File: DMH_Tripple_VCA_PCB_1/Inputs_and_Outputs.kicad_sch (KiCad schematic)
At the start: 0 parts

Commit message: Schematic in progress
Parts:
- added J1, J10, J2, J3, J4, J5, J6, J7, J8, J9: TS_Jack_6.35mm_Sw, SynthStuff:CUI_MJ-63052A, symbol SynthStuff:TS_Jack_6.35mm_Sw
- added J200: IDC_02x05, SynthStuff:IDC-Header_2x05_P2.54mm_Vertical_BackBone, symbol SynthStuff:BackBone_Connector_10Pin
- added J50, J60, J70: Conn_01x06, Connector_PinSocket_2.54mm:PinSocket_1x06_P2.54mm_Vertical, symbol Connector_Generic:Conn_01x06
- added R53, R54, R55: 20k, Resistor_THT:R_Axial_DIN0207_L6.3mm_D2.5mm_P7.62mm_Horizontal, symbol Device:R_US
- added RV4, RV5, RV6: 100k, SynthStuff:Potentiometer_Alpha_RD901F-40-00D_Single_Vertical, symbol Device:R_Potentiometer_US
- added SW1, SW2, SW3: SW_SPDT_321, symbol Switch:SW_SPDT_321
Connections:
- new net: J200.7 (Pin_7), J9.TN
- new net: J2.TN, J200.2 (Pin_2)
- new net: J1.TN, J200.1 (Pin_1)
- new net: J200.10 (Pin_10), J6.TN
- new net: J200.3 (Pin_3), J3.TN
- new net: J200.4 (Pin_4), J4.TN
- new net: J200.5 (Pin_5), J5.TN
- new net: J10.TN, J200.6 (Pin_6)
- new net: J200.8 (Pin_8), J8.TN
- new net: J200.9 (Pin_9), J7.TN
- new net: R54.1, RV5.1
- new net: R53.1, RV4.1
- new net: R55.1, RV6.1
- new net +12V: J50.1 (Pin_1), J60.1 (Pin_1), J70.1 (Pin_1), R53.2, R54.2, R55.2
- new net CV A Jack: J3.T
- new net CV B Jack: J6.T
- new net CV C Jack: J9.T
- new net GND: J1.S, J10.S, J2.S, J3.S, J4.S, J5.S, J50.5 (Pin_5), J50.6 (Pin_6), J6.S, J60.5 (Pin_5), J60.6 (Pin_6), J7.S, J70.5 (Pin_5), J70.6 (Pin_6), J8.S, J9.S, RV4.3, RV5.3, RV6.3
- new net Input A Jack: J1.T
- new net Input B Jack: J4.T
- new net Input C Jack: J7.T
- new net Mix Out Jack: J10.T
- new net Mute A Switch: J50.2 (Pin_2), SW1.3 (A)
- new net Mute B Switch: J60.2 (Pin_2), SW2.3 (A)
- new net Mute C Switch: J70.2 (Pin_2), SW3.3 (A)
- new net Offset A Pot: J50.4 (Pin_4), RV4.2
- new net Offset B Pot: J60.4 (Pin_4), RV5.2
- new net Offset C Pot: J70.4 (Pin_4), RV6.2
- new net Output A Jack: J2.T, J50.3 (Pin_3), SW1.2 (B)
- new net Output B Jack: J5.T, J60.3 (Pin_3), SW2.2 (B)
- new net Output C Jack: J70.3 (Pin_3), J8.T, SW3.2 (B)
- no-connect marks 0 -> 3
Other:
- note added: "PCB 2"

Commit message: Finished Schematic
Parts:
- removed SW2, SW3: SW_SPDT_321, symbol Switch:SW_SPDT_321
- added D3, D4, D5: LED_BGKR, LED_THT:LED_D5.0mm-4_RGB, symbol Device:LED_BGKR
- added R56, R58, R60: 220R, Resistor_THT:R_Axial_DIN0207_L6.3mm_D2.5mm_P7.62mm_Horizontal, symbol Device:R_US
- added R57, R59, R61: 330R, Resistor_THT:R_Axial_DIN0207_L6.3mm_D2.5mm_P7.62mm_Horizontal, symbol Device:R_US
- added SW2, SW3: SW_DPDT, SynthStuff:PinHeader_2x03_P2.54mm_Vertical_142536, symbol SynthStuff:Switch_DPDT
- SW1: value SW_SPDT_321 -> SW_DPDT; footprint (none) -> SynthStuff:PinHeader_2x03_P2.54mm_Vertical_142536; symbol Switch:SW_SPDT_321 -> SynthStuff:Switch_DPDT
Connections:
- net +12V: now also SW1.5 (B), SW2.5 (B), SW3.5 (B)
- net GND: now also D3.3 (K), D4.3 (K), D5.3 (K)
- net Mute A Switch: now also SW1.1 (A); no longer SW1.3 (A)
- net Mute B Switch: now also SW2.1 (A)
- net Mute C Switch: now also SW3.1 (A)
- net Output B Jack: now also SW2.2 (B)
- net Output C Jack: now also SW3.2 (B)
- new net: D4.2 (GA), R58.1
- new net: D4.4 (RA), R59.1
- new net: R57.2, SW1.4 (A)
- new net: R56.2, SW1.6 (C)
- new net: R61.2, SW3.4 (A)
- new net: R60.2, SW3.6 (C)
- new net: D3.2 (GA), R56.1
- new net: R59.2, SW2.4 (A)
- new net: R58.2, SW2.6 (C)
- new net: D5.2 (GA), R60.1
- new net: D3.4 (RA), R57.1
- new net: D5.4 (RA), R61.1
- no-connect marks 3 -> 6
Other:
- moved on the sheet: R53, R54, R55, RV4, RV5, RV6

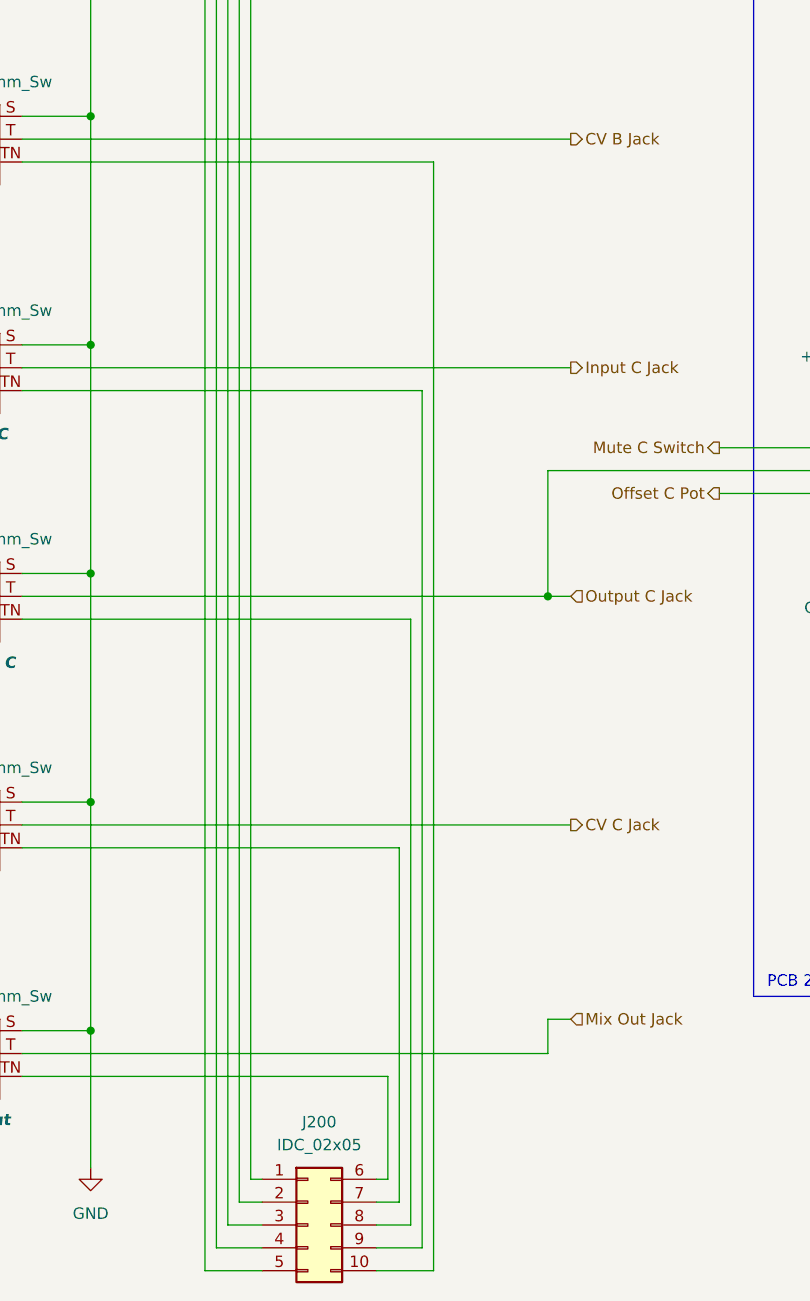
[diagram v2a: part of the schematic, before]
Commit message: PCB 1 component positioning ongoing
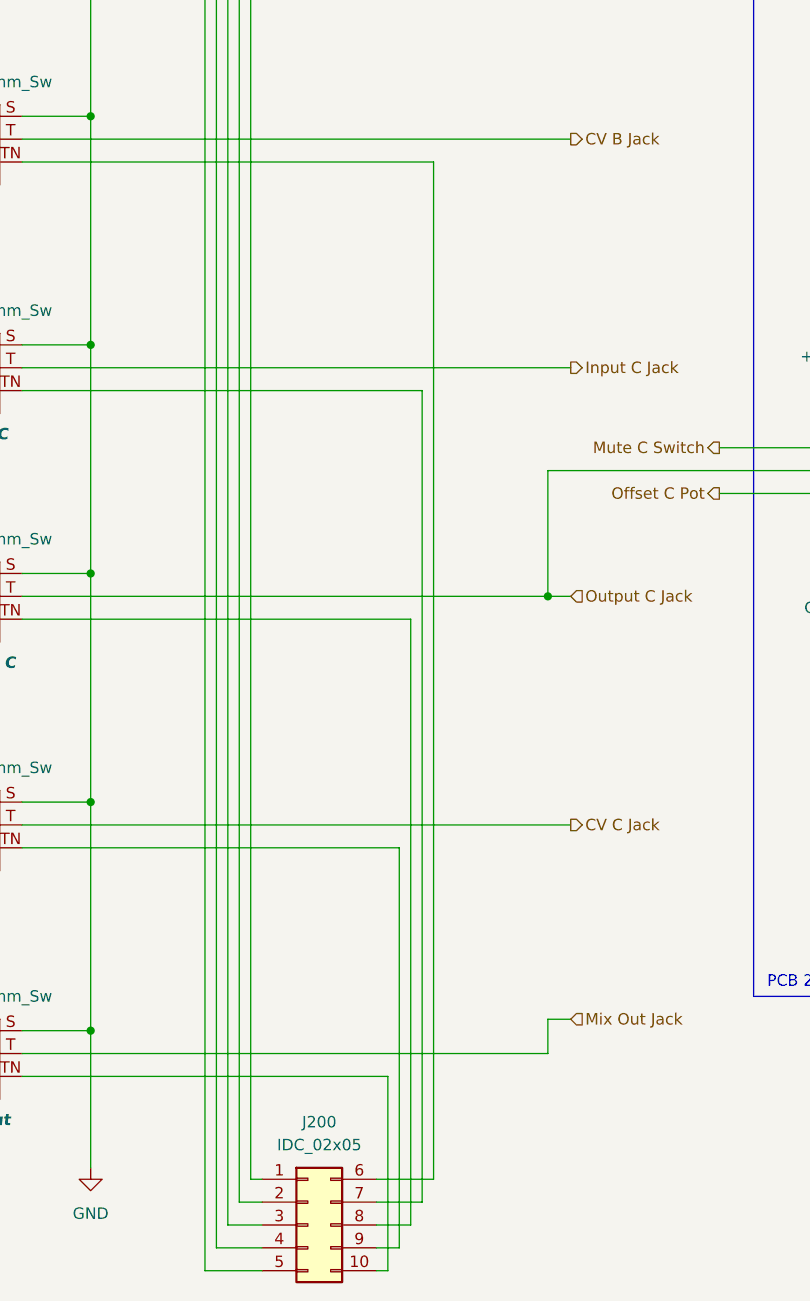
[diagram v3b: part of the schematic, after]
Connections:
- net at J9.TN: now also J200.9 (Pin_9); no longer J200.7 (Pin_7)
- net at J200.10 (Pin_10): now also J10.TN; no longer J6.TN
- net at J200.6 (Pin_6): now also J6.TN; no longer J10.TN
- net at J7.TN: now also J200.7 (Pin_7); no longer J200.9 (Pin_9)
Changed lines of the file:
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@@
+	(wire
+		(pts
+			(xy 69.85 270.51) (xy 74.93 270.51)
+		)
+		(stroke
+			(width 0)
+			(type default)
+		)
+	)
 	(wire
 		(pts
@@
 	(wire
 		(pts
+			(xy 69.85 267.97) (xy 76.2 267.97)
+		)
+		(stroke
+			(width 0)
+			(type default)
+		)
+	)
+	(wire
+		(pts
+			(xy 69.85 273.05) (xy 73.66 273.05)
+		)
+		(stroke
+			(width 0)
+			(type default)
+		)
+	)
+	(wire
+		(pts
 			(xy 176.53 146.05) (xy 179.07 146.05)
 		)
@@
 	(wire
 		(pts
-			(xy 72.39 270.51) (xy 72.39 231.14)
+			(xy 72.39 231.14) (xy 72.39 275.59)
 		)
 		(stroke
@@
 	(wire
 		(pts
-			(xy 69.85 278.13) (xy 76.2 278.13)
-		)
-		(stroke
-			(width 0)
-			(type default)
-		)
-	)
-	(wire
-		(pts
 			(xy 176.53 106.68) (xy 189.23 106.68)
 		)
@@
 	(wire
 		(pts
+			(xy 71.12 256.54) (xy 71.12 278.13)
+		)
+		(stroke
+			(width 0)
+			(type default)
+		)
+	)
+	(wire
+		(pts
 			(xy 52.07 104.14) (xy 30.48 104.14)
 		)
@@
 	(wire
 		(pts
-			(xy 71.12 256.54) (xy 71.12 267.97)
-		)
-		(stroke
-			(width 0)
-			(type default)
-		)
-	)
-	(wire
-		(pts
 			(xy 38.1 266.7) (xy 38.1 251.46)
 		)
@@
 	(wire
 		(pts
-			(xy 69.85 275.59) (xy 74.93 275.59)
-		)
-		(stroke
-			(width 0)
-			(type default)
-		)
-	)
-	(wire
-		(pts
 			(xy 158.75 195.58) (xy 158.75 209.55)
 		)
@@
 	(wire
 		(pts
+			(xy 72.39 275.59) (xy 69.85 275.59)
+		)
+		(stroke
+			(width 0)
+			(type default)
+		)
+	)
+	(wire
+		(pts
 			(xy 121.92 118.11) (xy 119.38 118.11)
 		)
@@
 	(wire
 		(pts
-			(xy 76.2 154.94) (xy 76.2 278.13)
+			(xy 76.2 154.94) (xy 76.2 267.97)
 		)
 		(stroke
@@
 	(wire
 		(pts
-			(xy 69.85 273.05) (xy 73.66 273.05)
-		)
-		(stroke
-			(width 0)
-			(type default)
-		)
-	)
-	(wire
-		(pts
 			(xy 146.05 67.31) (xy 146.05 72.39)
 		)
@@
 	(wire
 		(pts
-			(xy 74.93 180.34) (xy 74.93 275.59)
+			(xy 74.93 180.34) (xy 74.93 270.51)
 		)
 		(stroke
@@
 	(wire
 		(pts
-			(xy 69.85 267.97) (xy 71.12 267.97)
-		)
-		(stroke
-			(width 0)
-			(type default)
-		)
-	)
-	(wire
-		(pts
 			(xy 38.1 175.26) (xy 38.1 149.86)
 		)
@@
 	(wire
 		(pts
-			(xy 69.85 270.51) (xy 72.39 270.51)
-		)
-		(stroke
+			(xy 71.12 278.13) (xy 69.85 278.13)
+		)
+		(stroke

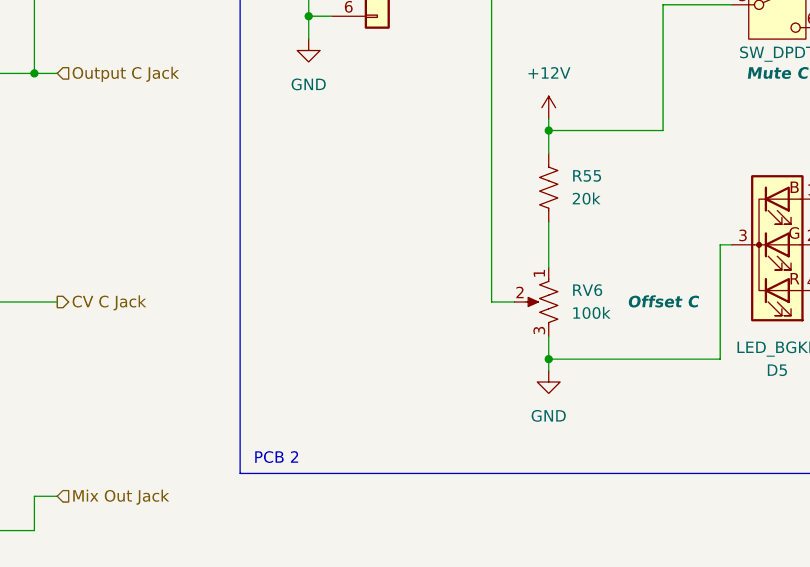
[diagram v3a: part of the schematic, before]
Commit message: PCB 1 component positioning in progress
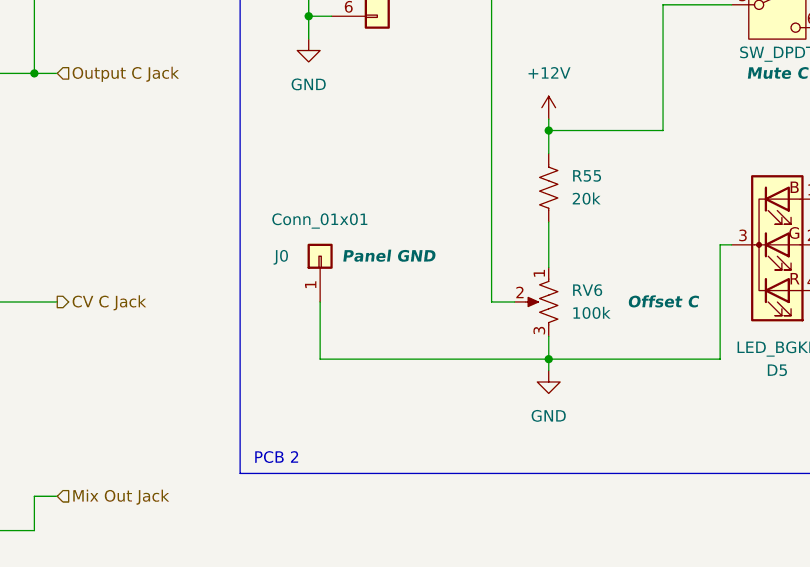
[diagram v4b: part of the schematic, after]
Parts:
- added J0: Conn_01x01, Connector_PinHeader_2.54mm:PinHeader_1x01_P2.54mm_Vertical, symbol Connector_Generic:Conn_01x01
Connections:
- net GND: now also J0.1 (Pin_1)
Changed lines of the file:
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@@
 	(wire
 		(pts
+			(xy 120.65 228.6) (xy 120.65 234.95)
+		)
+		(stroke
+			(width 0)
+			(type default)
+		)
+	)
+	(wire
+		(pts
 			(xy 121.92 194.31) (xy 119.38 194.31)
 		)
@@
 	(wire
 		(pts
+			(xy 120.65 234.95) (xy 146.05 234.95)
+		)
+		(stroke
+			(width 0)
+			(type default)
+		)
+	)
+	(wire
+		(pts
 			(xy 152.4 189.23) (xy 121.92 189.23)
 		)
@@
 					(unit 1)
 				)
+			)
+		)
+	)
+	(symbol
+		(lib_id "Connector_Generic:Conn_01x01")
+		(at 120.65 223.52 90)
+		(unit 1)
+		(exclude_from_sim no)
+		(in_bom yes)
+		(on_board no)
+		(dnp no)
+		(property "Reference" "J0"
+			(at 115.57 223.52 90)
+			(effects
+				(font
+					(size 1.27 1.27)
+				)
+				(justify right)
+			)
+		)
+		(property "Value" "Conn_01x01"
+			(at 120.65 219.456 90)
+			(effects
+				(font
+					(size 1.27 1.27)
+				)
+			)
+		)
+		(property "Footprint" "Connector_PinHeader_2.54mm:PinHeader_1x01_P2.54mm_Vertical"
+			(at 120.65 223.52 0)
+			(effects
+				(font
+					(size 1.27 1.27)
+				)
+				(hide yes)
+			)
+		)
+		(property "Datasheet" "~"
+			(at 120.65 223.52 0)
+			(effects
+				(font
+					(size 1.27 1.27)
+				)
+				(hide yes)
+			)
+		)
+		(property "Description" "Generic connector, single row, 01x01, script generated (kicad-library-utils/schlib/autogen/connector/)"
+			(at 120.65 223.52 0)
+			(effects
+				(font
+					(size 1.27 1.27)
+				)
+				(hide yes)
+			)
+		)
+		(property "Function" "Panel GND"
+			(at 128.27 223.52 90)
+			(effects
+				(font
+					(size 1.27 1.27)
+					(thickness 0.254)
+					(bold yes)
+					(italic yes)
+				)
+			)
+		)
+		(pin "1"
+		)
+		(instances
+			(project "DMH_Tripple_VCA_PCB_1"
+				(path "/58f4306d-5387-4983-bb08-41a2313fd315/ce3fef8b-9f1d-4178-b50b-4a046c030679"
+					(reference "J0")
+					(unit 1)
+				)

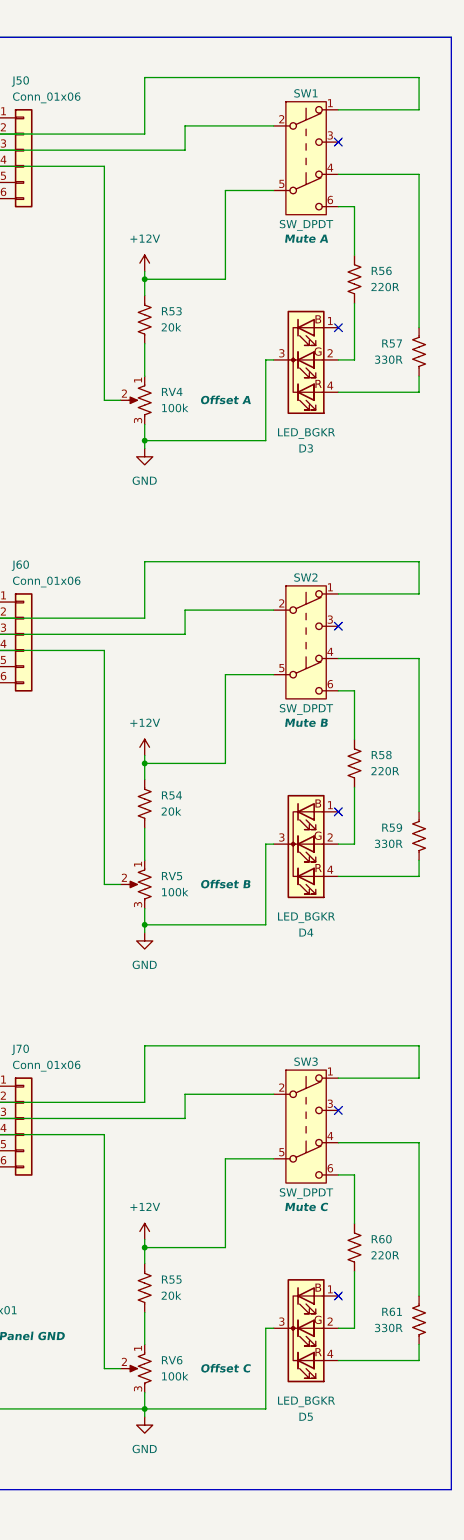
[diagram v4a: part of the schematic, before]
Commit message: Changed LEDs to bi-color
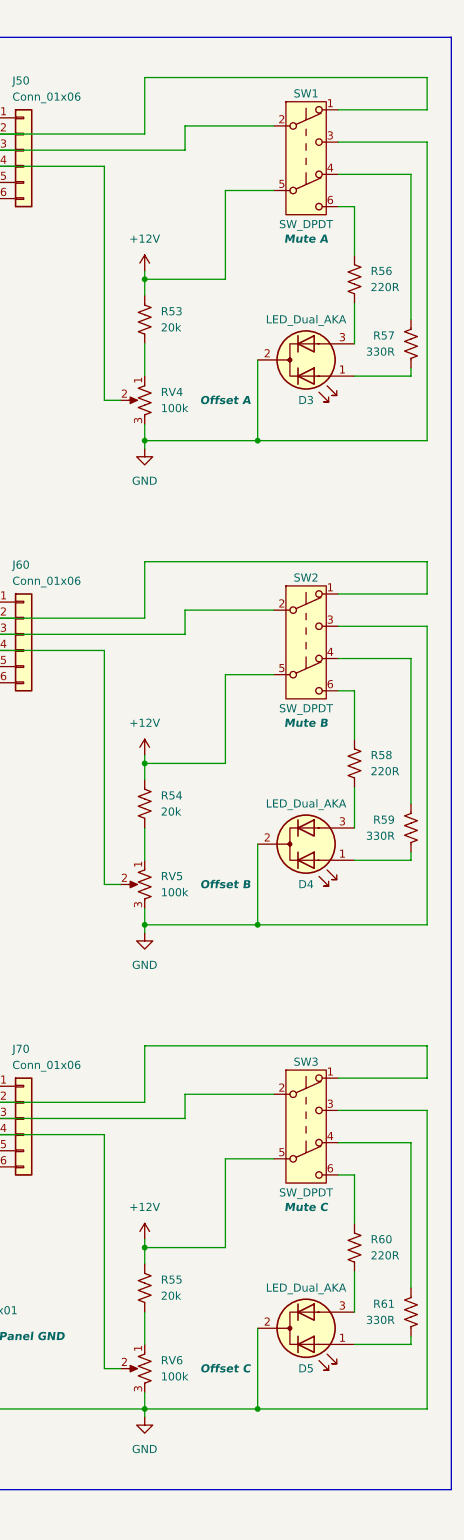
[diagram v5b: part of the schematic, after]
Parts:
- D3, D4, D5: value LED_BGKR -> LED_Dual_AKA; footprint LED_THT:LED_D5.0mm-4_RGB -> SynthStuff:LED_D3.0mm-2color; symbol Device:LED_BGKR -> Device:LED_Dual_AKA
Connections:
- net GND: now also D3.2 (K), D4.2 (K), D5.2 (K), SW1.3 (C), SW2.3 (C), SW3.3 (C); no longer D3.3 (K), D4.3 (K), D5.3 (K)
- net at D4.1 (A1): now also R59.1
- net at R58.1: now also D4.3 (A2); no longer D4.2 (GA)
- net at R56.1: now also D3.3 (A2); no longer D3.2 (GA)
- net at R60.1: now also D5.3 (A2); no longer D5.2 (GA)
- net at D3.1 (A1): now also R57.1
- net at D5.1 (A1): now also R61.1
- no-connect marks 6 -> 0
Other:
- moved on the sheet: R57, R59, R61

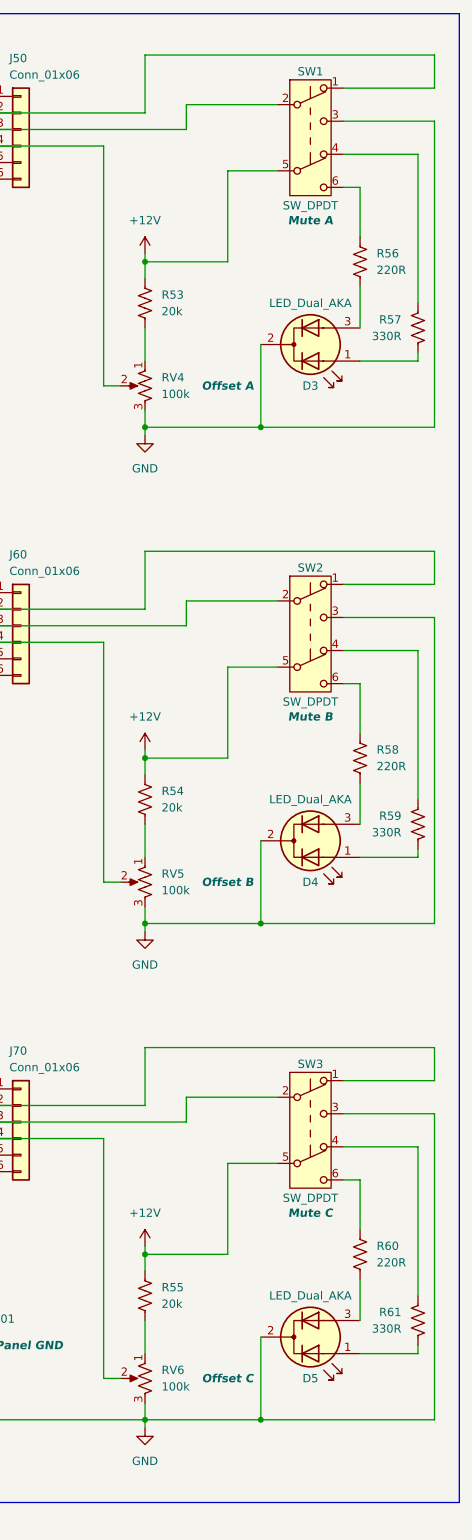
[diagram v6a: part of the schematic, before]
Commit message: Corrected header locations and placed pcb2 comps
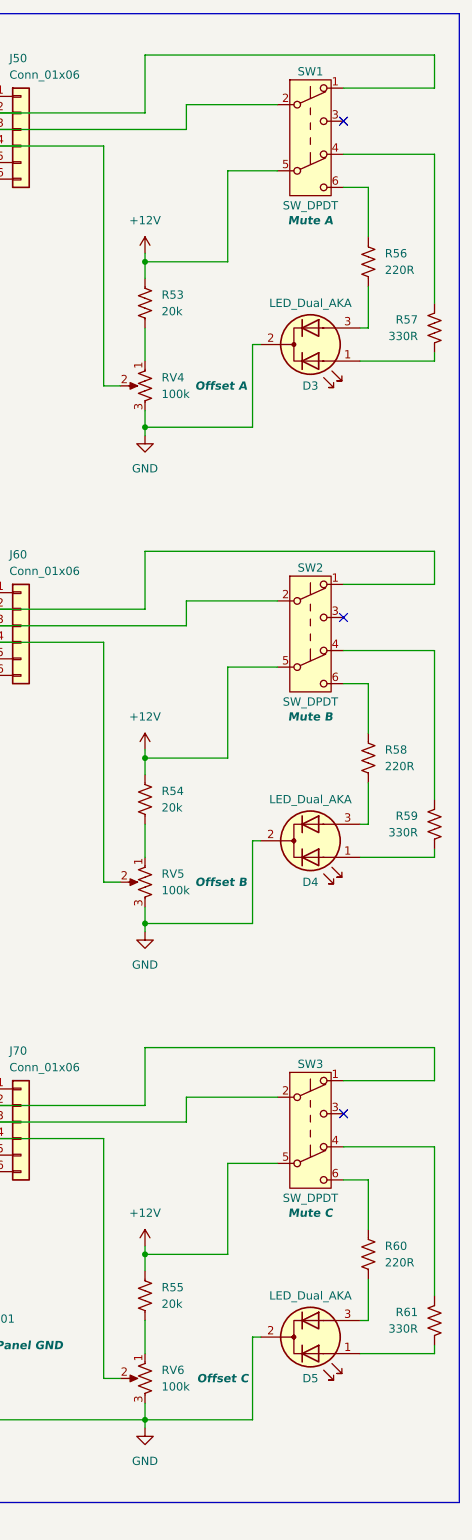
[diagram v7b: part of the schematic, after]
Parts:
- SW1, SW2, SW3: footprint SynthStuff:PinHeader_2x03_P2.54mm_Vertical_142536 -> SynthStuff:Toggle_Switch_2_Poles_THT
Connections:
- net GND: no longer SW1.3 (C), SW2.3 (C), SW3.3 (C)
- no-connect marks 0 -> 3
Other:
- moved on the sheet: R56, R57, R58, R59, R60, R61

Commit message: Routed PCB 2
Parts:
- J0: now not fitted; now left out of the parts list
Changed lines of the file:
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@@
 		(unit 1)
 		(exclude_from_sim no)
-		(in_bom yes)
+		(in_bom no)
 		(on_board no)
-		(dnp no)
+		(dnp yes)
 		(property "Reference" "J0"
 			(at 115.57 223.52 90)
